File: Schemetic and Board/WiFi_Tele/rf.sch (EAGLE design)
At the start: 26 parts

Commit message: changed mixer
Changed mixer from HMC213B to LT5522 due to stock issues
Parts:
- removed C5: 10pF, rcl:C-EUC0805
- removed C6: 100nF, rcl:C-EUC0805
- removed C7: 1nF, rcl:C-EUC0805
- removed L2: 1nH, Passives:COILCRAFT_INDUCTOR0603/1608M
- removed LNA_LO: ADL5523ACPZ-R7CP_8_2-M, ADL5523ACPZ-R7:ADL5523ACPZ-R7CP_8_2-M
- removed MIXER: HMC213BMS8E, HMC213B:HMC213BMS8E
- removed R1, R2: 33k, rcl:R-EU_R0805
- removed R4: 1.33k, rcl:R-EU_R0805
- added L3: 4.7nH, Passives:L2012M
- added U1: LT5522EUF, LT5522:LT5522EUF
- C4: value 10pF -> 1000uF; device rcl:C-EUC0805 -> rcl:CPOL-US153CLV-1010
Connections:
- removed net IF: MIXER.IF, R1.1
- removed net IF_AA: C5.1, IF.1, R2.2
- removed net N$6: L2.P$2, LNA_LO.RFIN
- removed net N$7: C10.1, L2.P$1, VCO1.OUT
- net 5V: now also C4.+, U1.EN, U1.VCC1, U1.VCC2; no longer C6.2, C7.2, LNA_LO.VPOS, R4.2
- net GND: now also C4.-, L3.2, U1.GND, U1.GND_2, U1.GND_3, U1.LO-, U1.NC, U1.NC_2, U1.NC_3, U1.NC_4, U1.NC_5, U1.RF+; no longer C4.2, C5.2, C6.1, C7.1, IF.2, LNA_LO.EP, MIXER.GND, MIXER.GND_2, MIXER.GND_3, MIXER.GND_4
- net LO_AMPED: now also C10.1, VCO1.OUT; no longer LNA_LO.RFOUT
- net LO_FILTERED: now also U1.LO+; no longer MIXER.LO
- net N$3: now also IF.1, U1.IF+; no longer LNA_LO.VBIAS, R4.1
- net N$4: now also IF.2, U1.IF-; no longer C4.1, R1.2, R2.1
- net RF_FILTERED: now also L3.1, U1.RF-; no longer MIXER.RF
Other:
- moved on the sheet: BPF_LO, C1, C10, C2, C3, IF, VCO1

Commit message: rf schematic v2
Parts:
- added C5: 0.01uF, rcl:C-EUC0805
- added C6: 3.3uF, rcl:C-EUC0805
- added U$1: ETC4-1-2TR, ETC4-1-2TR:ETC4-1-2TR
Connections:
- new net N$6: U$1.SECONDARY_1, U1.IF+
- new net N$7: IF.2, U$1.PRIMARY_4
- net 5V: now also C5.1, C6.1, U$1.SECONDARY_CT
- net GND: now also C5.2, C6.2, SV1.1, SV1.3, SV1.5; no longer SV1.4
- net N$3: now also U$1.PRIMARY_5; no longer U1.IF+
- net N$4: now also U$1.SECONDARY_3; no longer IF.2
- net VCO_TUNE: now also SV1.4; no longer SV1.5
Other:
- moved on the sheet: IF
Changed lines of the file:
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@@
 <drawing>
 <settings>
-<setting alwaysvectorfont="yes"/>
+<setting alwaysvectorfont="no"/>
 <setting verticaltext="up"/>
 </settings>
@@
 <part name="C4" library="rcl" library_urn="urn:adsk.eagle:library:334" deviceset="CPOL-US" device="153CLV-1010" package3d_urn="urn:adsk.eagle:package:23413/1" value="1000uF"/>
 <part name="SUPPLY13" library="supply2" library_urn="urn:adsk.eagle:library:372" deviceset="GND" device=""/>
+<part name="U$1" library="ETC4-1-2TR" deviceset="ETC4-1-2TR" device=""/>
+<part name="SUPPLY19" library="supply2" library_urn="urn:adsk.eagle:library:372" deviceset="GND" device=""/>
+<part name="C5" library="rcl" library_urn="urn:adsk.eagle:library:334" deviceset="C-EU" device="C0805" package3d_urn="urn:adsk.eagle:package:23617/2" value="0.01uF"/>
+<part name="C6" library="rcl" library_urn="urn:adsk.eagle:library:334" deviceset="C-EU" device="C0805" package3d_urn="urn:adsk.eagle:package:23617/2" value="3.3uF"/>
 </parts>
 <sheets>
@@
 <instance part="SUPPLY18" gate="GND" x="7.62" y="33.02"/>
 <instance part="ANT" gate="G$1" x="-10.16" y="43.18"/>
-<instance part="IF" gate="G$1" x="309.88" y="43.18" rot="MR0"/>
+<instance part="IF" gate="G$1" x="350.52" y="45.72" rot="MR0"/>
 <instance part="SUPPLY20" gate="GND" x="-7.62" y="33.02"/>
 <instance part="SV1" gate="G$1" x="-96.52" y="63.5"/>
@@
 <instance part="SUPPLY6" gate="GND" x="243.84" y="68.58"/>
 <instance part="SUPPLY7" gate="GND" x="248.92" y="53.34" rot="R270"/>
-<instance part="SUPPLY9" gate="GND" x="248.92" y="43.18" rot="R270"/>
+<instance part="SUPPLY9" gate="GND" x="251.46" y="35.56"/>
 <instance part="SUPPLY11" gate="GND" x="289.56" y="40.64" rot="R90"/>
 <instance part="SUPPLY14" gate="GND" x="292.1" y="50.8" rot="R90"/>
@@
 <instance part="C4" gate="G$1" x="-48.26" y="81.28"/>
 <instance part="SUPPLY13" gate="GND" x="-48.26" y="66.04"/>
+<instance part="U$1" gate="G$1" x="314.96" y="45.72" rot="R180"/>
+<instance part="SUPPLY19" gate="GND" x="-71.12" y="55.88"/>
+<instance part="C5" gate="G$1" x="238.76" y="45.72"/>
+<instance part="C6" gate="G$1" x="226.06" y="45.72"/>
 </instances>
 <busses>
@@
 <pinref part="SUPPLY20" gate="GND" pin="GND"/>
 <wire x1="-7.62" y1="40.64" x2="-7.62" y2="35.56" width="0.1524" layer="91"/>
-</segment>
-<segment>
-<pinref part="SV1" gate="G$1" pin="4"/>
-<wire x1="-88.9" y1="66.04" x2="-76.2" y2="66.04" width="0.1524" layer="91"/>
-<label x="-81.28" y="66.04" size="1.778" layer="95"/>
 </segment>
 <segment>
@@
 <pinref part="U1" gate="A" pin="NC_4"/>
 <pinref part="SUPPLY9" gate="GND" pin="GND"/>
+<wire x1="251.46" y1="38.1" x2="251.46" y2="40.64" width="0.1524" layer="91"/>
+<pinref part="C6" gate="G$1" pin="2"/>
+<pinref part="C5" gate="G$1" pin="2"/>
+<wire x1="251.46" y1="40.64" x2="251.46" y2="43.18" width="0.1524" layer="91"/>
+<wire x1="226.06" y1="40.64" x2="238.76" y2="40.64" width="0.1524" layer="91"/>
+<wire x1="238.76" y1="40.64" x2="251.46" y2="40.64" width="0.1524" layer="91"/>
+<junction x="238.76" y="40.64"/>
+<junction x="251.46" y="40.64"/>
 </segment>
 <segment>
@@
 <pinref part="SUPPLY13" gate="GND" pin="GND"/>
 </segment>
+<segment>
+<pinref part="SV1" gate="G$1" pin="5"/>
+<wire x1="-88.9" y1="68.58" x2="-86.36" y2="68.58" width="0.1524" layer="91"/>
+<wire x1="-86.36" y1="68.58" x2="-71.12" y2="68.58" width="0.1524" layer="91"/>
+<pinref part="SV1" gate="G$1" pin="3"/>
+<wire x1="-88.9" y1="63.5" x2="-71.12" y2="63.5" width="0.1524" layer="91"/>
+<wire x1="-71.12" y1="68.58" x2="-71.12" y2="63.5" width="0.1524" layer="91"/>
+<wire x1="-71.12" y1="63.5" x2="-71.12" y2="58.42" width="0.1524" layer="91"/>
+<junction x="-71.12" y="63.5"/>
+<pinref part="SV1" gate="G$1" pin="1"/>
+<wire x1="-71.12" y1="58.42" x2="-88.9" y2="58.42" width="0.1524" layer="91"/>
+<pinref part="SUPPLY19" gate="GND" pin="GND"/>
+<junction x="-71.12" y="58.42"/>
+</segment>
 </net>
 <net name="N$2" class="0">
@@
 </segment>
 <segment>
-<pinref part="SV1" gate="G$1" pin="5"/>
-<wire x1="-88.9" y1="68.58" x2="-76.2" y2="68.58" width="0.1524" layer="91"/>
-<label x="-81.28" y="68.58" size="1.778" layer="95"/>
+<pinref part="SV1" gate="G$1" pin="4"/>
+<wire x1="-88.9" y1="66.04" x2="-76.2" y2="66.04" width="0.1524" layer="91"/>
+<label x="-81.28" y="66.04" size="1.778" layer="95"/>
 </segment>
 </net>
@@
 <wire x1="248.92" y1="48.26" x2="241.3" y2="48.26" width="0.1524" layer="91"/>
 <junction x="248.92" y="48.26"/>
-<label x="241.3" y="48.26" size="1.778" layer="95"/>
+<label x="233.68" y="48.26" size="1.778" layer="95"/>
 <pinref part="U1" gate="A" pin="EN"/>
 <wire x1="251.46" y1="50.8" x2="248.92" y2="50.8" width="0.1524" layer="91"/>
 <wire x1="248.92" y1="50.8" x2="248.92" y2="48.26" width="0.1524" layer="91"/>
+<pinref part="C5" gate="G$1" pin="1"/>
+<wire x1="241.3" y1="48.26" x2="238.76" y2="48.26" width="0.1524" layer="91"/>
+<pinref part="C6" gate="G$1" pin="1"/>
+<wire x1="238.76" y1="48.26" x2="226.06" y2="48.26" width="0.1524" layer="91"/>
+<junction x="238.76" y="48.26"/>
+<wire x1="226.06" y1="48.26" x2="223.52" y2="48.26" width="0.1524" layer="91"/>
+<junction x="226.06" y="48.26"/>
 </segment>
 <segment>
@@
 <wire x1="-48.26" y1="83.82" x2="-48.26" y2="88.9" width="0.1524" layer="91"/>
 <label x="-48.26" y="88.9" size="1.778" layer="95"/>
+</segment>
+<segment>
+<pinref part="U$1" gate="G$1" pin="SECONDARY_CT"/>
+<wire x1="307.34" y1="45.72" x2="304.8" y2="45.72" width="0.1524" layer="91"/>
+<wire x1="304.8" y1="45.72" x2="304.8" y2="60.96" width="0.1524" layer="91"/>
+<wire x1="304.8" y1="60.96" x2="307.34" y2="60.96" width="0.1524" layer="91"/>
+<wire x1="307.34" y1="60.96" x2="307.34" y2="68.58" width="0.1524" layer="91"/>
+<label x="307.34" y="66.04" size="1.778" layer="95"/>
 </segment>
 </net>
@@
 </segment>
 </net>
+<net name="N$4" class="0">
+<segment>
+<pinref part="U1" gate="A" pin="IF-"/>
+<wire x1="287.02" y1="43.18" x2="299.72" y2="43.18" width="0.1524" layer="91"/>
+<wire x1="299.72" y1="43.18" x2="299.72" y2="40.64" width="0.1524" layer="91"/>
+<pinref part="U$1" gate="G$1" pin="SECONDARY_3"/>
+<wire x1="299.72" y1="40.64" x2="307.34" y2="40.64" width="0.1524" layer="91"/>
+</segment>
+</net>
+<net name="N$6" class="0">
+<segment>
+<pinref part="U1" gate="A" pin="IF+"/>
+<wire x1="287.02" y1="45.72" x2="299.72" y2="45.72" width="0.1524" layer="91"/>
+<wire x1="299.72" y1="45.72" x2="299.72" y2="50.8" width="0.1524" layer="91"/>
+<pinref part="U$1" gate="G$1" pin="SECONDARY_1"/>
+<wire x1="299.72" y1="50.8" x2="307.34" y2="50.8" width="0.1524" layer="91"/>
+</segment>
+</net>
 <net name="N$3" class="0">
 <segment>
-<pinref part="U1" gate="A" pin="IF+"/>
+<pinref part="U$1" gate="G$1" pin="PRIMARY_5"/>
+<wire x1="322.58" y1="50.8" x2="342.9" y2="50.8" width="0.1524" layer="91"/>
+<wire x1="342.9" y1="50.8" x2="342.9" y2="48.26" width="0.1524" layer="91"/>
 <pinref part="IF" gate="G$1" pin="1"/>
-<wire x1="287.02" y1="45.72" x2="307.34" y2="45.72" width="0.1524" layer="91"/>
-</segment>
-</net>
-<net name="N$4" class="0">
-<segment>
-<pinref part="U1" gate="A" pin="IF-"/>
-<wire x1="287.02" y1="43.18" x2="304.8" y2="43.18" width="0.1524" layer="91"/>
-<wire x1="304.8" y1="43.18" x2="304.8" y2="40.64" width="0.1524" layer="91"/>
+<wire x1="342.9" y1="48.26" x2="347.98" y2="48.26" width="0.1524" layer="91"/>
+</segment>
+</net>
+<net name="N$7" class="0">
+<segment>
+<pinref part="U$1" gate="G$1" pin="PRIMARY_4"/>
+<wire x1="322.58" y1="40.64" x2="342.9" y2="40.64" width="0.1524" layer="91"/>
+<wire x1="342.9" y1="40.64" x2="342.9" y2="43.18" width="0.1524" layer="91"/>
 <pinref part="IF" gate="G$1" pin="2"/>
-<wire x1="304.8" y1="40.64" x2="307.34" y2="40.64" width="0.1524" layer="91"/>
-</segment>
-</net>
+<wire x1="342.9" y1="43.18" x2="347.98" y2="43.18" width="0.1524" layer="91"/>
+</segment>
+</net>

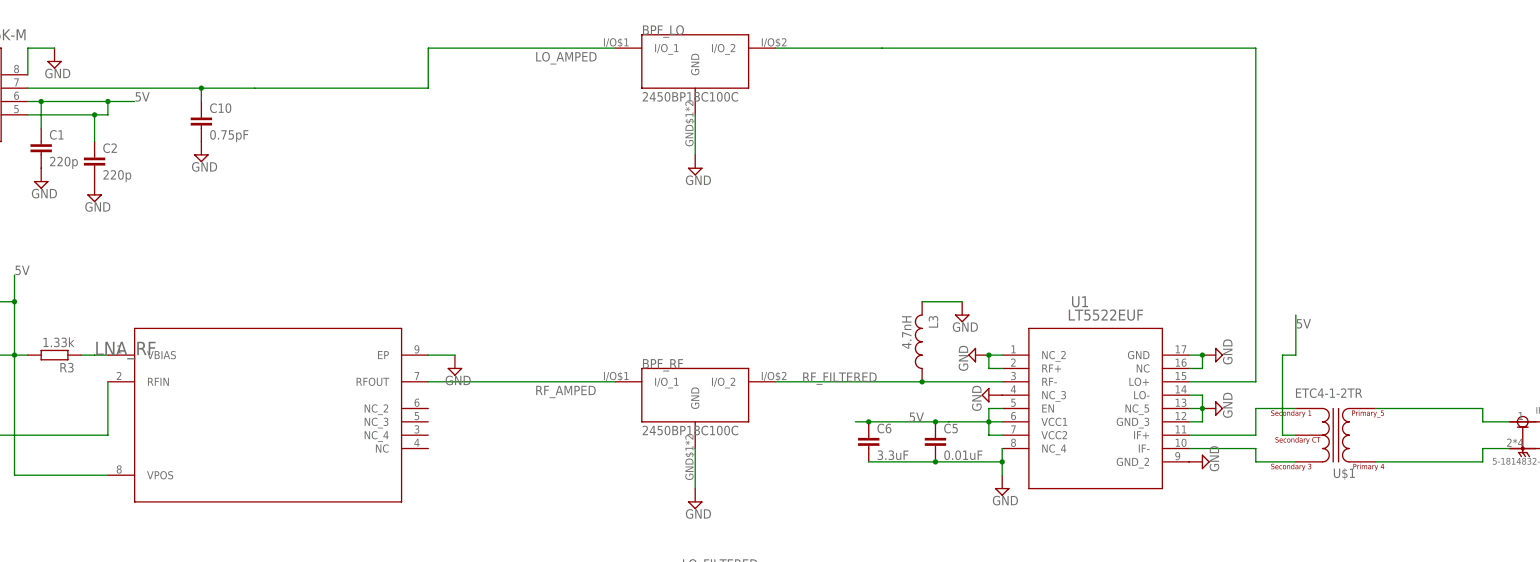
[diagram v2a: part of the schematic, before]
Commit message: Start FPGA board routing
Routed SMA -> VGA1 matched diff pairs
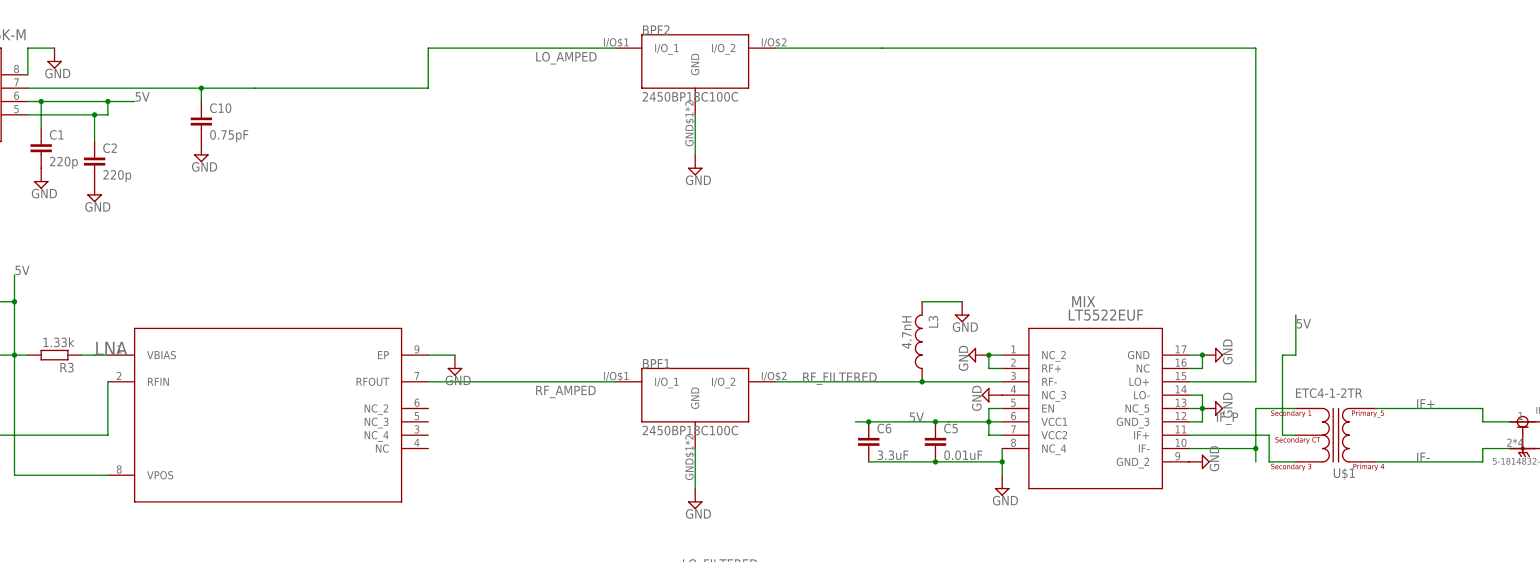
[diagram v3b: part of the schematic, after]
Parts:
- renumbered BPF_LO to BPF2, BPF_RF to BPF1, LNA_RF to LNA, U1 to MIX
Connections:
- net N$3 renamed IF+
- net N$7 renamed IF-
- removed net N$6: MIX.IF+, U$1.SECONDARY_1
- new net IF_P: MIX.IF+, U$1.SECONDARY_3
- net N$4: now also U$1.SECONDARY_1; no longer U$1.SECONDARY_3
